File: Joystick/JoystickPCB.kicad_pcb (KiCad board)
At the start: 2 copper layers, 62 x 42 mm, 21 parts, among them J1 JST B6B-PH-SM4-TB, J2 JST B4B-PH-SM4-TB, J3 JST B4B-PH-SM4-TB, J4 JST B3B-PH-SM4-TB, U1 MIC5225-1.8YM5-TR, U2 ADS1115IDGSR, U3 ICM-20948

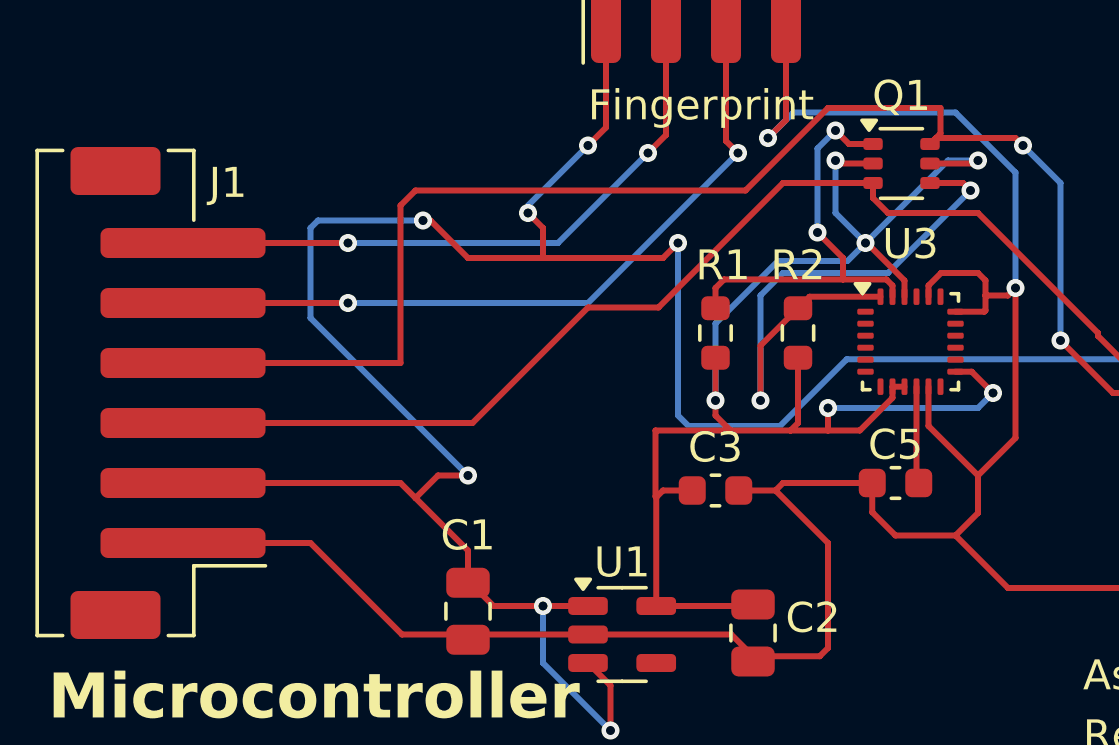
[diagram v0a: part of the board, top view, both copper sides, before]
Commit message: Changed R and C sizes and added part numbers
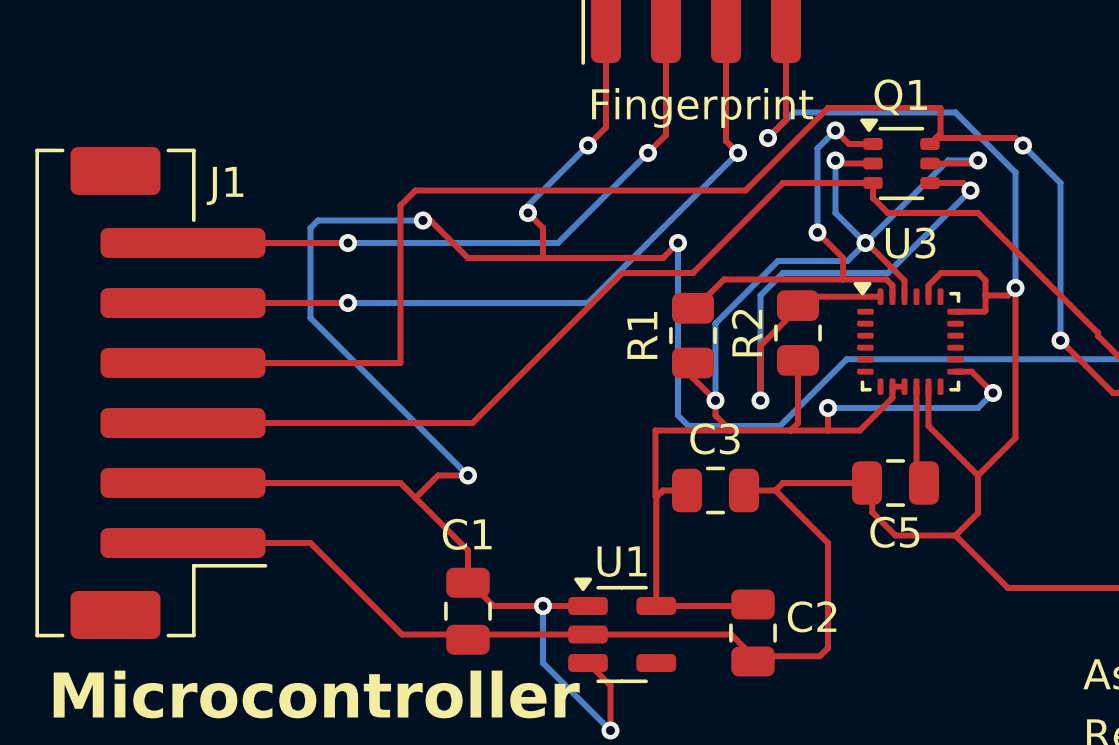
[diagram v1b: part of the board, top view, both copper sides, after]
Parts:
- C3, C5: footprint Capacitor_SMD:C_0603_1608Metric -> Capacitor_SMD:C_0805_2012Metric
- R1, R2: footprint Resistor_SMD:R_0603_1608Metric -> Resistor_SMD:R_0805_2012Metric
- moved R1 0.76 mm to (149.5, 66.1)

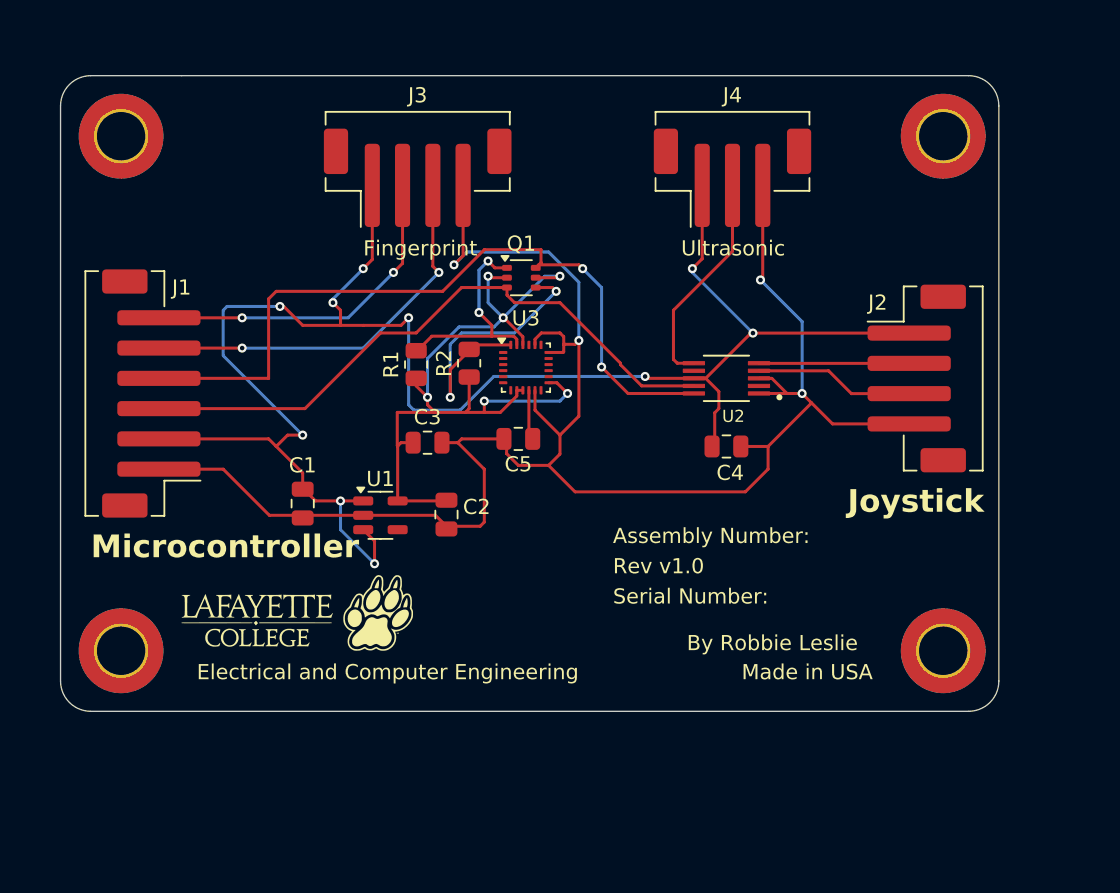
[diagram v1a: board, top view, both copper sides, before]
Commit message: Switch mounting holes to M3 ISO 7380
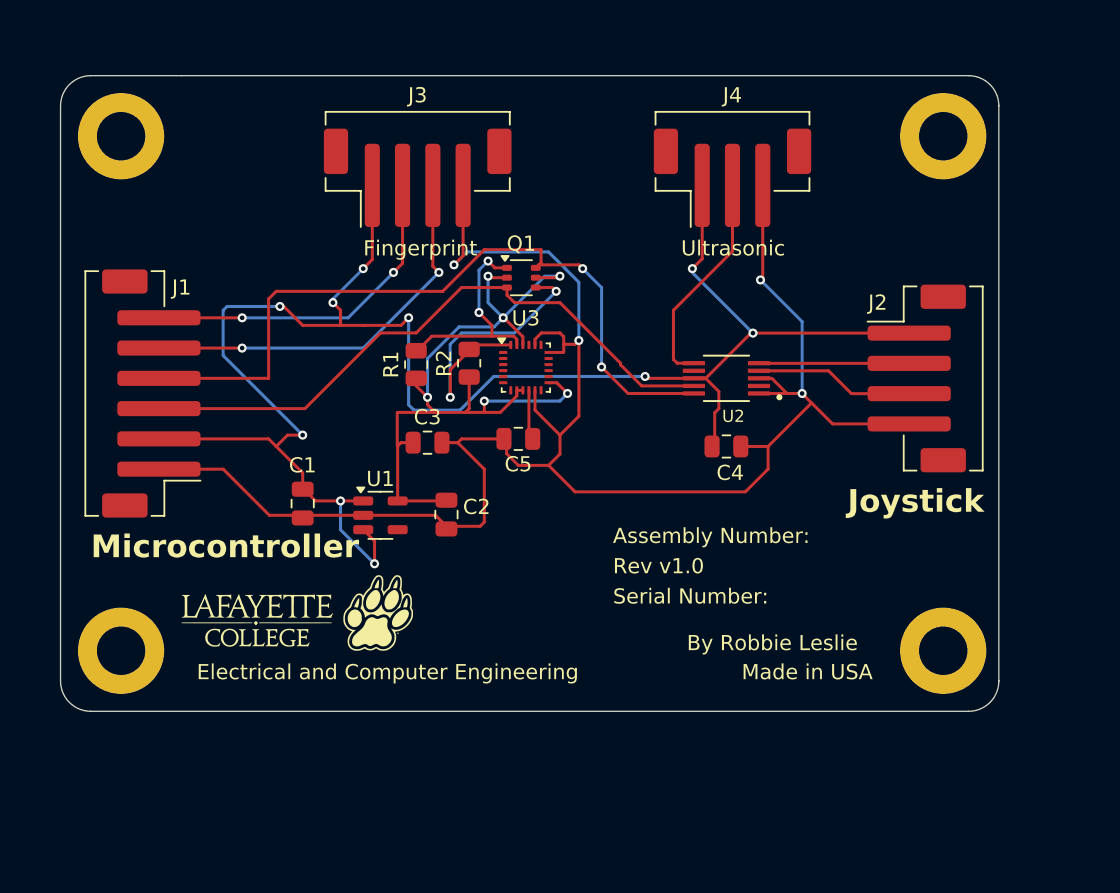
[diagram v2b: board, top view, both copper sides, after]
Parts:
- H1, H2, H3, H4: footprint MountingHole:MountingHole_3.2mm_M3_DIN965_Pad_TopBottom -> MountingHole:MountingHole_3.2mm_M3_ISO7380_Pad
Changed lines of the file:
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@@
 			)
 		)
-		(property "Manufacturer Part Number" ""
+		(property "Manufacturer Part Number" "GRM21BR61C106KE15K"
 			(at 0 0 0)
 			(unlocked yes)
@@
 			)
 		)
-		(property "Manufacturer Part Number" ""
+		(property "Manufacturer Part Number" "GRM21BR61C106KE15K"
 			(at 0 0 -90)
 			(unlocked yes)
@@
 		)
 	)
-	(footprint "MountingHole:MountingHole_3.2mm_M3_DIN965_Pad_TopBottom"
+	(footprint "MountingHole:MountingHole_3.2mm_M3_ISO7380_Pad"
 		(layer "F.Cu")
 		(at 184.325 85)
-		(descr "Mounting Hole 3.2mm, M3, DIN965")
-		(tags "mounting hole 3.2mm m3 din965")
+		(descr "Mounting Hole 3.2mm, M3, ISO7380")
+		(tags "mounting hole 3.2mm m3 iso7380")
 		(property "Reference" "H4"
-			(at 0 -3.8 0)
+			(at 0 -3.85 0)
 			(layer "F.SilkS")
 			(hide yes)
@@
 		)
 		(property "Value" "MountingHole"
-			(at 0 3.8 0)
+			(at 0 3.85 0)
 			(layer "F.Fab")
 			(effects
@@
 			)
 		)
-		(property "Footprint" "MountingHole:MountingHole_3.2mm_M3_DIN965_Pad_TopBottom"
+		(property "Footprint" "MountingHole:MountingHole_3.2mm_M3_ISO7380_Pad"
 			(at 0 0 0)
 			(unlocked yes)
@@
 		(fp_circle
 			(center 0 0)
-			(end 2.8 0)
+			(end 2.85 0)
 			(stroke
 				(width 0.15)
@@
 		(fp_circle
 			(center 0 0)
-			(end 3.05 0)
+			(end 3.1 0)
 			(stroke
 				(width 0.05)
@@
 		(pad "1" thru_hole circle
 			(at 0 0)
-			(size 3.6 3.6)
+			(size 5.7 5.7)
 			(drill 3.2)
 			(layers "*.Cu" "*.Mask")
 			(remove_unused_layers no)
 		)
-		(pad "1" connect circle
-			(at 0 0)
-			(size 5.6 5.6)
-			(layers "F.Cu" "F.Mask")
-		)
-		(pad "1" connect circle
-			(at 0 0)
-			(size 5.6 5.6)
-			(layers "B.Cu" "B.Mask")
-		)
 	)
 	(footprint "Capacitor_SMD:C_0805_2012Metric"
@@
 		)
 	)
-	(footprint "MountingHole:MountingHole_3.2mm_M3_DIN965_Pad_TopBottom"
+	(footprint "MountingHole:MountingHole_3.2mm_M3_ISO7380_Pad"
 		(layer "F.Cu")
 		(at 184.325 51)
-		(descr "Mounting Hole 3.2mm, M3, DIN965")
-		(tags "mounting hole 3.2mm m3 din965")
+		(descr "Mounting Hole 3.2mm, M3, ISO7380")
+		(tags "mounting hole 3.2mm m3 iso7380")
 		(property "Reference" "H2"
-			(at 0 -3.8 0)
+			(at 0 -3.85 0)
 			(layer "F.SilkS")
 			(hide yes)
@@
 		)
 		(property "Value" "MountingHole"
-			(at 0 3.8 0)
+			(at 0 3.85 0)
 			(layer "F.Fab")
 			(effects
@@
 			)
 		)
-		(property "Footprint" "MountingHole:MountingHole_3.2mm_M3_DIN965_Pad_TopBottom"
+		(property "Footprint" "MountingHole:MountingHole_3.2mm_M3_ISO7380_Pad"
 			(at 0 0 0)
 			(unlocked yes)
@@
 		(fp_circle
 			(center 0 0)
-			(end 2.8 0)
+			(end 2.85 0)
 			(stroke
 				(width 0.15)
@@
 		(fp_circle
 			(center 0 0)
-			(end 3.05 0)
+			(end 3.1 0)
 			(stroke
 				(width 0.05)
@@
 		(pad "1" thru_hole circle
 			(at 0 0)
-			(size 3.6 3.6)
+			(size 5.7 5.7)
 			(drill 3.2)
 			(layers "*.Cu" "*.Mask")
 			(remove_unused_layers no)
 		)
-		(pad "1" connect circle
-			(at 0 0)
-			(size 5.6 5.6)
-			(layers "F.Cu" "F.Mask")
-		)
-		(pad "1" connect circle
-			(at 0 0)
-			(size 5.6 5.6)
-			(layers "B.Cu" "B.Mask")
-		)
 	)
-	(footprint "MountingHole:MountingHole_3.2mm_M3_DIN965_Pad_TopBottom"
+	(footprint "MountingHole:MountingHole_3.2mm_M3_ISO7380_Pad"
 		(layer "F.Cu")
 		(at 130 85)
-		(descr "Mounting Hole 3.2mm, M3, DIN965")
-		(tags "mounting hole 3.2mm m3 din965")
+		(descr "Mounting Hole 3.2mm, M3, ISO7380")
+		(tags "mounting hole 3.2mm m3 iso7380")
 		(property "Reference" "H3"
-			(at 0 -3.8 0)
+			(at 0 -3.85 0)
 			(layer "F.SilkS")
 			(hide yes)
@@
 		)
 		(property "Value" "MountingHole"
-			(at 0 3.8 0)
+			(at 0 3.85 0)
 			(layer "F.Fab")
 			(effects
@@
 			)
 		)
-		(property "Footprint" "MountingHole:MountingHole_3.2mm_M3_DIN965_Pad_TopBottom"
+		(property "Footprint" "MountingHole:MountingHole_3.2mm_M3_ISO7380_Pad"
 			(at 0 0 0)
 			(unlocked yes)
@@
 		(fp_circle
 			(center 0 0)
-			(end 2.8 0)
+			(end 2.85 0)
 			(stroke
 				(width 0.15)
@@
 		(fp_circle
 			(center 0 0)
-			(end 3.05 0)
+			(end 3.1 0)
 			(stroke
 				(width 0.05)
@@
 		(pad "1" thru_hole circle
 			(at 0 0)
-			(size 3.6 3.6)
+			(size 5.7 5.7)
 			(drill 3.2)
 			(layers "*.Cu" "*.Mask")
 			(remove_unused_layers no)
 		)
-		(pad "1" connect circle
-			(at 0 0)
-			(size 5.6 5.6)
-			(layers "F.Cu" "F.Mask")
-		)
-		(pad "1" connect circle
-			(at 0 0)
-			(size 5.6 5.6)
-			(layers "B.Cu" "B.Mask")
-		)
 	)
 	(footprint "Package_TO_SOT_SMD:SOT-363_SC-70-6"
@@
 		)
 	)
-	(footprint "MountingHole:MountingHole_3.2mm_M3_DIN965_Pad_TopBottom"
+	(footprint "MountingHole:MountingHole_3.2mm_M3_ISO7380_Pad"
 		(layer "F.Cu")
 		(at 130 51)
-		(descr "Mounting Hole 3.2mm, M3, DIN965")
-		(tags "mounting hole 3.2mm m3 din965")
+		(descr "Mounting Hole 3.2mm, M3, ISO7380")
+		(tags "mounting hole 3.2mm m3 iso7380")
 		(property "Reference" "H1"
-			(at 0 -3.8 0)
+			(at 0 -3.85 0)
 			(layer "F.SilkS")
 			(hide yes)
@@
 		)
 		(property "Value" "MountingHole"
-			(at 0 3.8 0)
+			(at 0 3.85 0)
 			(layer "F.Fab")
 			(effects
@@
 			)
 		)
-		(property "Footprint" "MountingHole:MountingHole_3.2mm_M3_DIN965_Pad_TopBottom"
+		(property "Footprint" "MountingHole:MountingHole_3.2mm_M3_ISO7380_Pad"
 			(at 0 0 0)
 			(unlocked yes)
@@
 		(fp_circle
 			(center 0 0)
-			(end 2.8 0)
+			(end 2.85 0)
 			(stroke
 				(width 0.15)
@@
 		(fp_circle
 			(center 0 0)
-			(end 3.05 0)
+			(end 3.1 0)
 			(stroke
 				(width 0.05)
@@
 		(pad "1" thru_hole circle
 			(at 0 0)
-			(size 3.6 3.6)
+			(size 5.7 5.7)
 			(drill 3.2)
 			(layers "*.Cu" "*.Mask")
 			(remove_unused_layers no)
 		)
-		(pad "1" connect circle
-			(at 0 0)
-			(size 5.6 5.6)
-			(layers "F.Cu" "F.Mask")
-		)
-		(pad "1" connect circle
-			(at 0 0)
-			(size 5.6 5.6)
-			(layers "B.Cu" "B.Mask")
-		)
 	)
 	(footprint "Connector_JST:JST_PH_B6B-PH-SM4-TB_1x06-1MP_P2.00mm_Vertical"
@@
 			)
 		)
-		(property "Manufacturer Part Number" ""
+		(property "Manufacturer Part Number" "GRM21BR61C106KE15K"
 			(at 0 0 -90)
 			(unlocked yes)

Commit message: Added fill zone
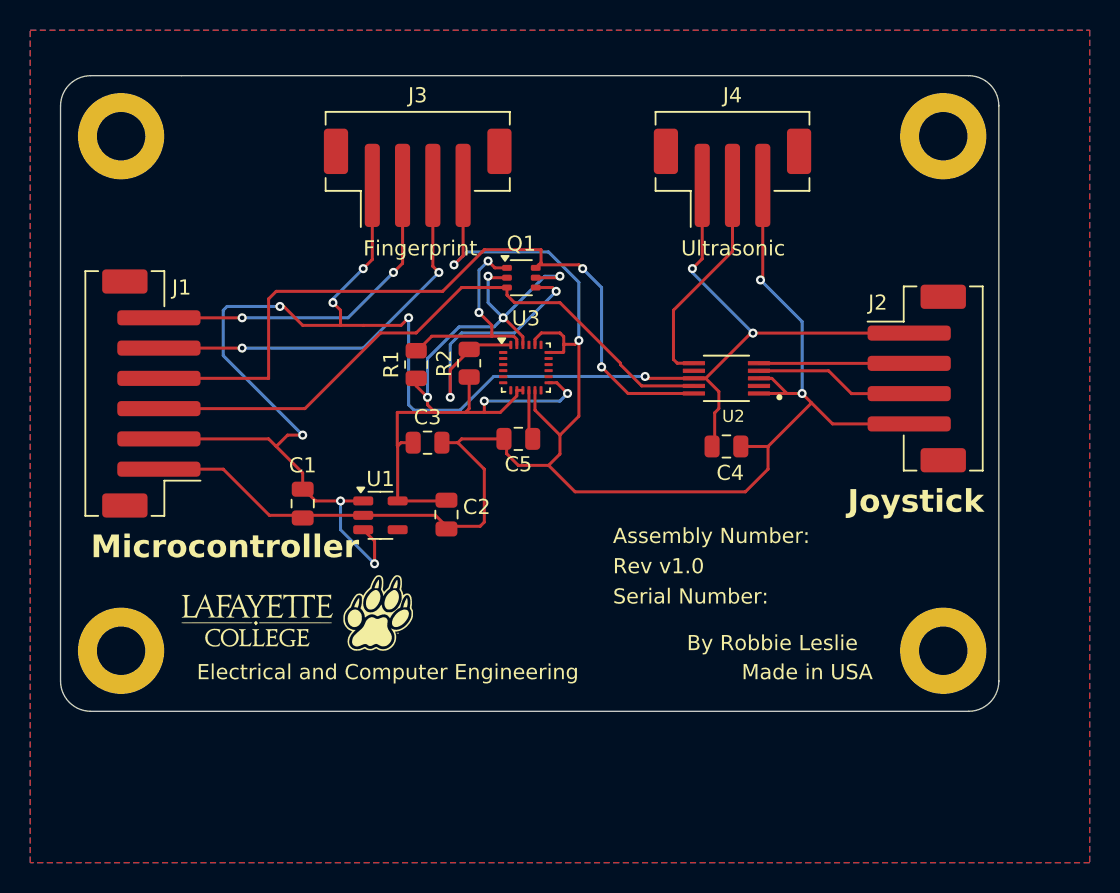
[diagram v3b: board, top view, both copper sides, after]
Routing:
- added copper zone on B.Cu, net /GND
- added copper zone on F.Cu, net /GND
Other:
- board text added: "2/2/25"
- board text removed: "1/28/25"
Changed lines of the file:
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@@
 		)
 	)
-	(gr_text "1/28/25"
+	(gr_text "2/2/25"
 		(at 207 194 0)
 		(layer "Cmts.User")
@@
 		(net 29)
 	)
+	(zone
+		(net 7)
+		(net_name "/GND")
+		(layers "F&B.Cu")
+		(hatch edge 0.5)
+		(connect_pads
+			(clearance 0.5)
+		)
+		(min_thickness 0.25)
+		(filled_areas_thickness no)
+		(fill yes
+			(thermal_gap 0.5)
+			(thermal_bridge_width 0.5)
+		)
+		(polygon
+			(pts
+				(xy 124 44) (xy 194 44) (xy 194 99) (xy 124 99)
+			)
+		)
+	)
 )

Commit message: Updated traces
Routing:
- net /3.3V: track 117.7 -> 120.2 mm
- net /GND: vias 4 -> 7
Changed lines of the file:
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@@
 	)
 	(segment
-		(start 147.15 64)
-		(end 149.5 64)
-		(width 0.2)
-		(layer "F.Cu")
-		(net 2)
-	)
-	(segment
-		(start 149.5 64)
-		(end 152.5 61)
+		(start 142.15 69)
+		(end 147.9 63.25)
+		(width 0.2)
+		(layer "F.Cu")
+		(net 2)
+	)
+	(segment
+		(start 164.401471 67.5)
+		(end 167.85 67.5)
+		(width 0.2)
+		(layer "F.Cu")
+		(net 2)
+	)
+	(segment
+		(start 153.25 61)
+		(end 155.5 61)
 		(width 0.2)
 		(layer "F.Cu")
@@
 	)
 	(segment
-		(start 164.401471 67.5)
-		(end 167.85 67.5)
-		(width 0.2)
-		(layer "F.Cu")
-		(net 2)
-	)
-	(segment
-		(start 142.15 69)
-		(end 147.15 64)
-		(width 0.2)
-		(layer "F.Cu")
-		(net 2)
-	)
-	(segment
 		(start 163 66)
 		(end 159 62)
@@
 	)
 	(segment
-		(start 152.5 61)
-		(end 155.5 61)
-		(width 0.2)
-		(layer "F.Cu")
-		(net 2)
-	)
-	(segment
 		(start 156 62)
 		(end 155.5 61.5)
@@
 	)
 	(segment
+		(start 147.9 63.25)
+		(end 151 63.25)
+		(width 0.2)
+		(layer "F.Cu")
+		(net 2)
+	)
+	(segment
+		(start 151 63.25)
+		(end 153.25 61)
+		(width 0.2)
+		(layer "F.Cu")
+		(net 2)
+	)
+	(segment
 		(start 163 66)
 		(end 163 66.098529)
@@
 	(segment
 		(start 172.15 66.5)
-		(end 176.75 66.5)
+		(end 175.25 66.5)
 		(width 0.2)
 		(layer "F.Cu")
@@
 	)
 	(segment
-		(start 176.75 66.5)
-		(end 178.26 68.01)
+		(start 176.76 68.01)
+		(end 182.075 68.01)
 		(width 0.2)
 		(layer "F.Cu")
@@
 	)
 	(segment
-		(start 178.26 68.01)
-		(end 182.075 68.01)
+		(start 175.25 66.5)
+		(end 176.76 68.01)
 		(width 0.2)
 		(layer "F.Cu")
@@
 	)
 	(via
+		(at 142 66.5)
+		(size 0.6)
+		(drill 0.3)
+		(layers "F.Cu" "B.Cu")
+		(free yes)
+		(net 7)
+	)
+	(via
 		(at 175 68)
 		(size 0.6)
 		(drill 0.3)
 		(layers "F.Cu" "B.Cu")
+		(net 7)
+	)
+	(via
+		(at 145.75 70)
+		(size 0.6)
+		(drill 0.3)
+		(layers "F.Cu" "B.Cu")
+		(free yes)
+		(net 7)
+	)
+	(via
+		(at 176.25 64.75)
+		(size 0.6)
+		(drill 0.3)
+		(layers "F.Cu" "B.Cu")
+		(free yes)
 		(net 7)
 	)
@@
 	)
 	(segment
-		(start 144.5 63.5)
-		(end 146 63.5)
-		(width 0.2)
-		(layer "F.Cu")
-		(net 9)
-	)
-	(segment
 		(start 146 77)
 		(end 146.75 77.75)
@@
 	)
 	(segment
+		(start 150 62.25)
+		(end 145.75 62.25)
+		(width 0.2)
+		(layer "F.Cu")
+		(net 9)
+	)
+	(segment
 		(start 142 63.5)
 		(end 140.75 62.25)
@@
 	)
 	(segment
-		(start 148.5 63.5)
-		(end 146 63.5)
-		(width 0.2)
-		(layer "F.Cu")
-		(net 9)
-	)
-	(segment
 		(start 168.4 54.25)
 		(end 168.4 59.1)
@@
 	)
 	(segment
+		(start 145.75 62.25)
+		(end 144.5 63.5)
+		(width 0.2)
+		(layer "F.Cu")
+		(net 9)
+	)
+	(segment
 		(start 142 74.5)
 		(end 142.25 74.5)
@@
 	)
 	(segment
-		(start 149 63)
-		(end 148.5 63.5)
-		(width 0.2)
-		(layer "F.Cu")
-		(net 9)
-	)
-	(segment
 		(start 140.25 71.5)
 		(end 141 70.75)
@@
 	)
 	(via
-		(at 149 63)
+		(at 150 62.25)
 		(size 0.6)
 		(drill 0.3)
@@
 		(drill 0.3)
 		(layers "F.Cu" "B.Cu")
+		(net 9)
+	)
+	(segment
+		(start 149.35 69.1)
+		(end 152.4 69.1)
+		(width 0.2)
+		(layer "B.Cu")
+		(net 9)
+	)
+	(segment
+		(start 154.625 66.875)
+		(end 164.625 66.875)
+		(width 0.2)
+		(layer "B.Cu")
+		(net 9)
+	)
+	(segment
+		(start 140.5 62.25)
+		(end 137 62.25)
+		(width 0.2)
+		(layer "B.Cu")
 		(net 9)
 	)
@@
 	)
 	(segment
+		(start 137 62.25)
+		(end 136.75 62.5)
+		(width 0.2)
+		(layer "B.Cu")
+		(net 9)
+	)
+	(segment
+		(start 144 61.75)
+		(end 144 62)
+		(width 0.2)
+		(layer "B.Cu")
+		(net 9)
+	)
+	(segment
+		(start 167.75 59.75)
+		(end 167.75 60.01)
+		(width 0.2)
+		(layer "B.Cu")
+		(net 9)
+	)
+	(segment
+		(start 150 62.25)
+		(end 149 63.25)
+		(width 0.2)
+		(layer "B.Cu")
+		(net 9)
+	)
+	(segment
+		(start 136.75 65.5)
+		(end 142 70.75)
+		(width 0.2)
+		(layer "B.Cu")
+		(net 9)
+	)
+	(segment
+		(start 149 63.25)
+		(end 149 68.75)
+		(width 0.2)
+		(layer "B.Cu")
+		(net 9)
+	)
+	(segment
 		(start 152.4 69.1)
 		(end 154.625 66.875)
@@
 	)
 	(segment
-		(start 140.5 62.25)
-		(end 137 62.25)
-		(width 0.2)
-		(layer "B.Cu")
-		(net 9)
-	)
-	(segment
-		(start 137 62.25)
-		(end 136.75 62.5)
-		(width 0.2)
-		(layer "B.Cu")
-		(net 9)
-	)
-	(segment
-		(start 154.625 66.875)
-		(end 164.625 66.875)
-		(width 0.2)
-		(layer "B.Cu")
-		(net 9)
-	)
-	(segment
-		(start 144 61.75)
-		(end 144 62)
-		(width 0.2)
-		(layer "B.Cu")
-		(net 9)
-	)
-	(segment
-		(start 167.75 59.75)
-		(end 167.75 60.01)
-		(width 0.2)
-		(layer "B.Cu")
-		(net 9)
-	)
-	(segment
-		(start 149.35 69.1)
-		(end 152.4 69.1)
-		(width 0.2)
-		(layer "B.Cu")
-		(net 9)
-	)
-	(segment
-		(start 136.75 65.5)
-		(end 142 70.75)
-		(width 0.2)
-		(layer "B.Cu")
-		(net 9)
-	)
-	(segment
 		(start 136.75 62.5)
 		(end 136.75 65.5)
@@
 		(width 0.2)
 		(layer "B.Cu")
-		(net 9)
-	)
-	(segment
-		(start 149 63)
-		(end 149 68.75)
-		(width 0.2)
-		(layer "B.Cu")
